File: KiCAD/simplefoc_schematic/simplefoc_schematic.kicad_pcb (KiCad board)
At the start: 2 copper layers, 52.3 x 49.1 mm, 61 parts, among them IC1 TMC6140-Trinamic, J1 Power Supply, J2 Motor Connector, J3 Sensor Connector, J5 Programming Port, J6 UART Port, J7 Servo, Q1 IRLR 2905, Q2 IRLR 2905, Q3 IRLR 2905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

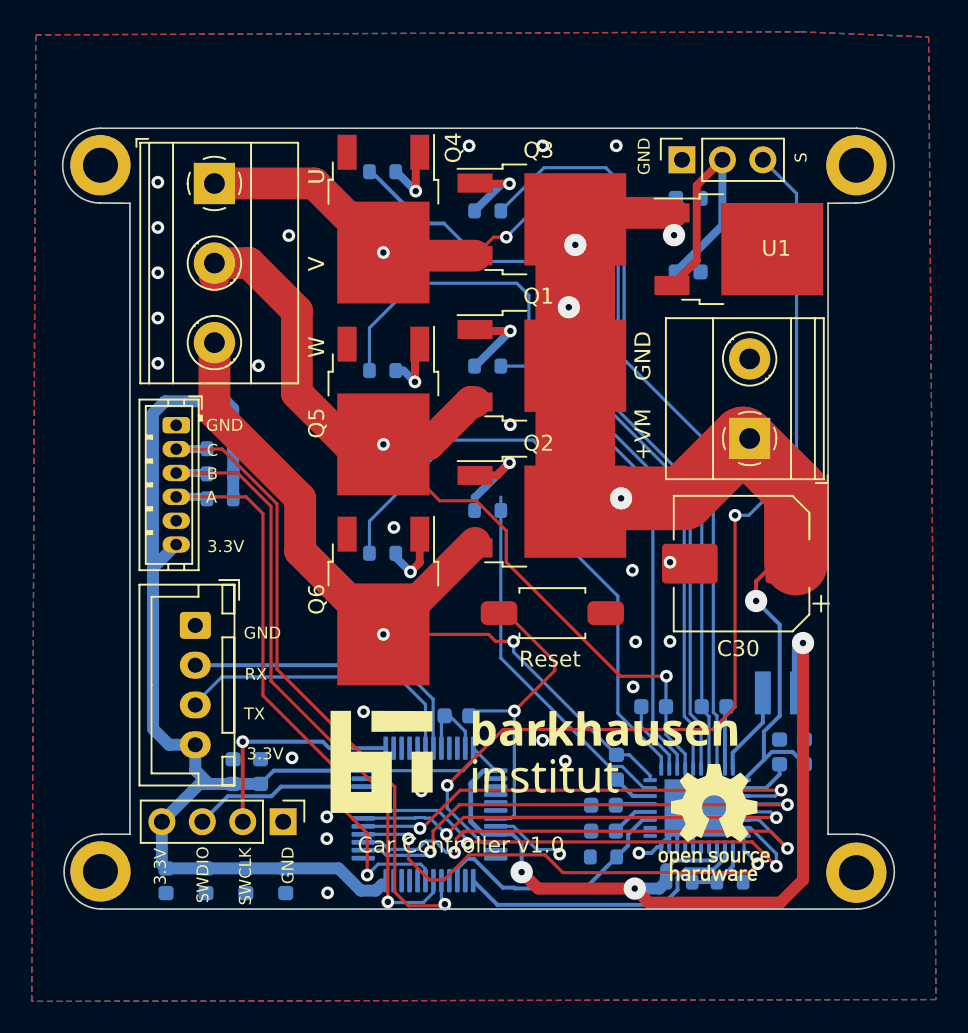
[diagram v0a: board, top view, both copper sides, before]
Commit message: Added second servo connection and fuse for servo
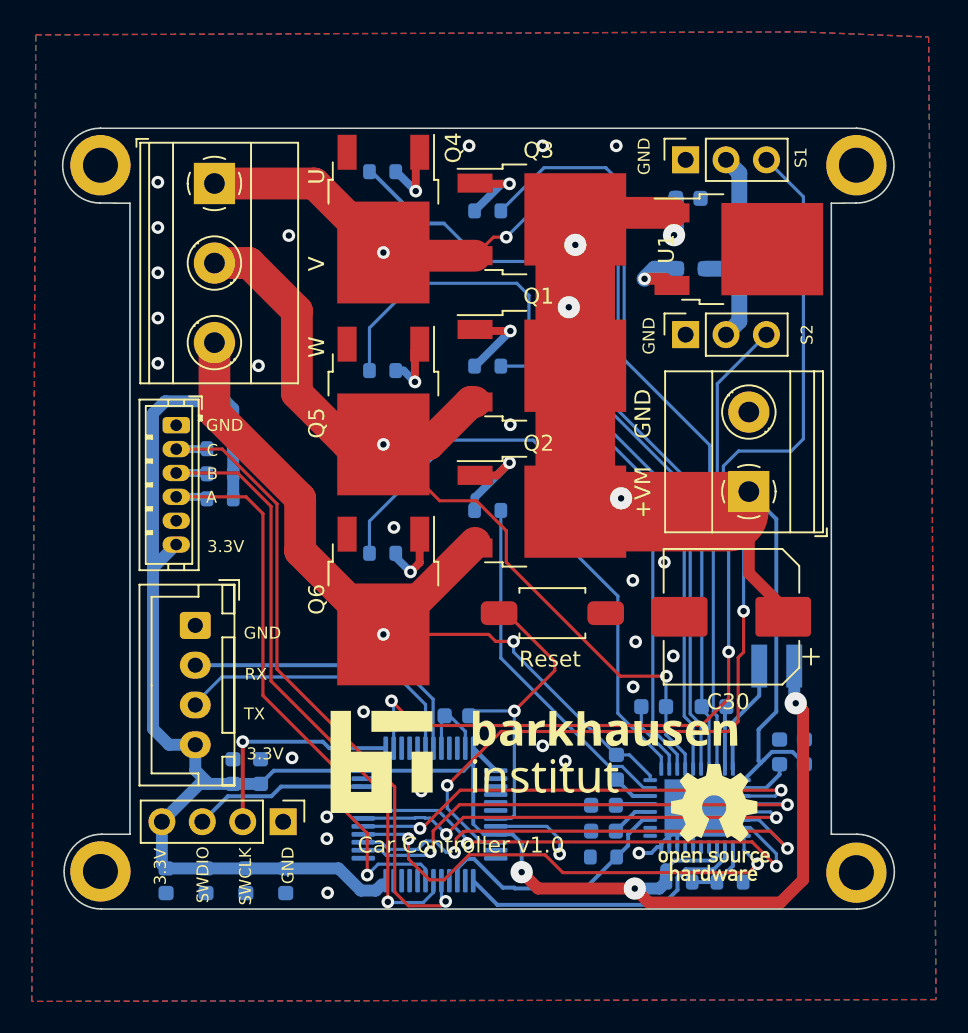
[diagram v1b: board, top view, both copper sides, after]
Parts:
- added F1: Polyfuse, Resistor_SMD:R_0603_1608Metric_Pad0.98x0.95mm_HandSolder, B.Cu at (113.3, 68.7)
- added J4: Servo, Connector_PinSocket_2.54mm:PinSocket_1x03_P2.54mm_Vertical, F.Cu at (112.9, 72.8)
- moved C19 3.99 mm to (117.1, 68.7)
- moved C30 3.40 mm to (115.8, 90.6)
- moved J1 3.34 mm to (116.9, 82.7)
- moved L1 1.70 mm to (118.6, 93.6)
- moved J7 0.23 mm to (112.9, 61.8)
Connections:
- net Servo renamed Servo1
- U1 pad 3: +5V -> Net-(U1-Pad3)
- U2 pad 38: unconnected-(U2-Pad38) -> Servo2
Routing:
- net Servo2: track 0.00 -> 50.0 mm, vias 0 -> 2
- net +BATT: track 80.2 -> 88.1 mm, vias 5 -> 4
- net +3.3V: track 134.8 -> 130.6 mm
- net Net-(U1-Pad3): track 0.00 -> 4.16 mm, vias 0 -> 1
- net +5V: track 17.5 -> 13.8 mm
- net Servo1: track 62.9 -> 66.3 mm
- net Net-(IC1-Pad10): track 5.57 -> 7.16 mm
- net V: track 60.1 -> 58.9 mm
- net GND: track 23.3 -> 24.2 mm
- net Net-(Q2-Pad1): track 5.59 -> 6.43 mm
- net HOUTW: track 22.9 -> 22.0 mm
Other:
- outline, holes or cut-outs redrawn
- board text added: "S1"
- board text added: "S2"
- board text removed: "S"

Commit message: Added polyfuse to battery input
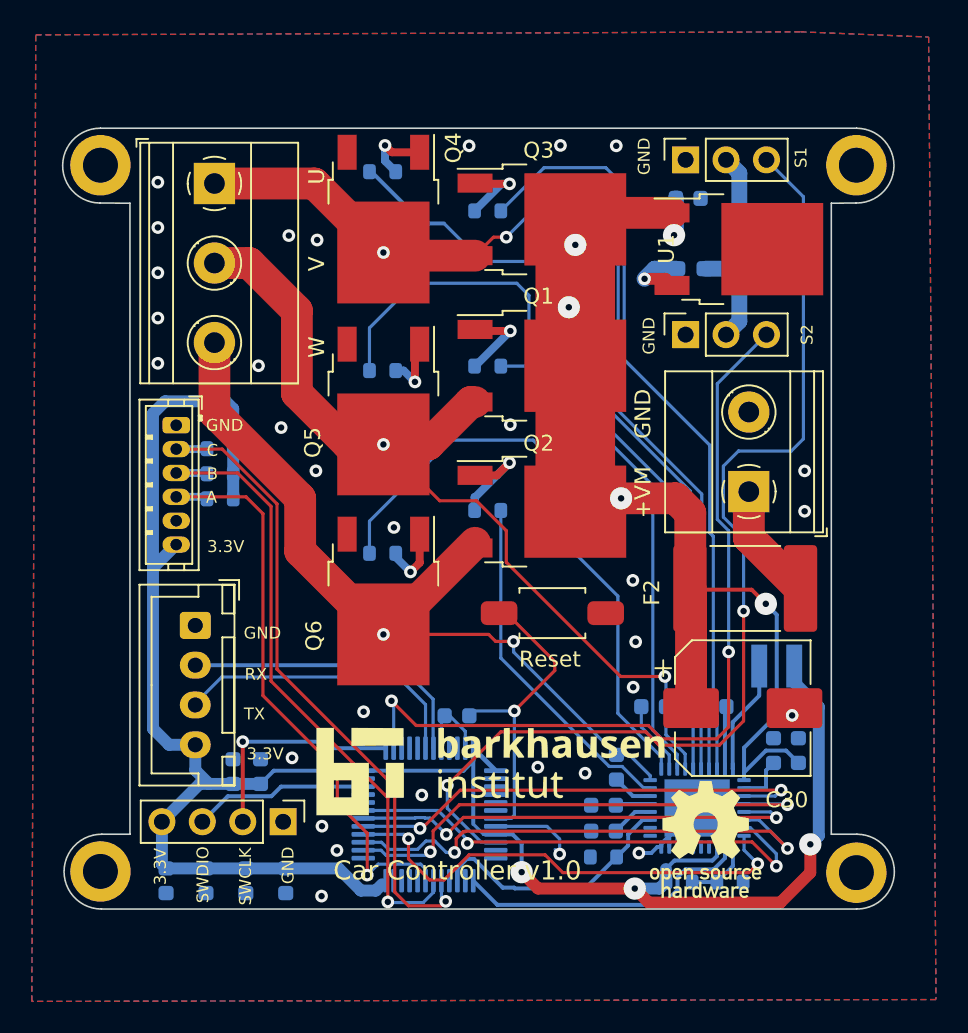
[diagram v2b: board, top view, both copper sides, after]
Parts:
- added F2: Polyfuse, Fuse:Fuse_2920_7451Metric_Pad2.10x5.45mm_HandSolder, F.Cu at (116.7, 88.8)
- F1: footprint Resistor_SMD:R_0603_1608Metric_Pad0.98x0.95mm_HandSolder -> Fuse:Fuse_0603_1608Metric_Pad1.05x0.95mm_HandSolder
- moved C30 5.78 mm to (116.5, 96.3), turned to 0 degrees
- moved G*** 2.79 mm to (100.6, 100.3)
- moved G*** 1.19 mm to (114.2, 104.5)
- moved C23 0.39 mm to (120.0, 99.0)
- moved C27 0.39 mm to (118.4, 99.0)
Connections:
- J1 pad 1: +BATT -> Net-(J1-Pad1)
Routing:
- net Net-(J1-Pad1): track 0.00 -> 7.52 mm
- net +BATT: track 88.1 -> 83.2 mm, vias 4 -> 5
- net Servo2: track 50.0 -> 51.7 mm
- net Servo1: track 66.3 -> 67.1 mm
- net +3.3V: track 130.6 -> 131.4 mm
- net GND: vias 27 -> 31

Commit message: Change to 4 Layer PCB with better grounding
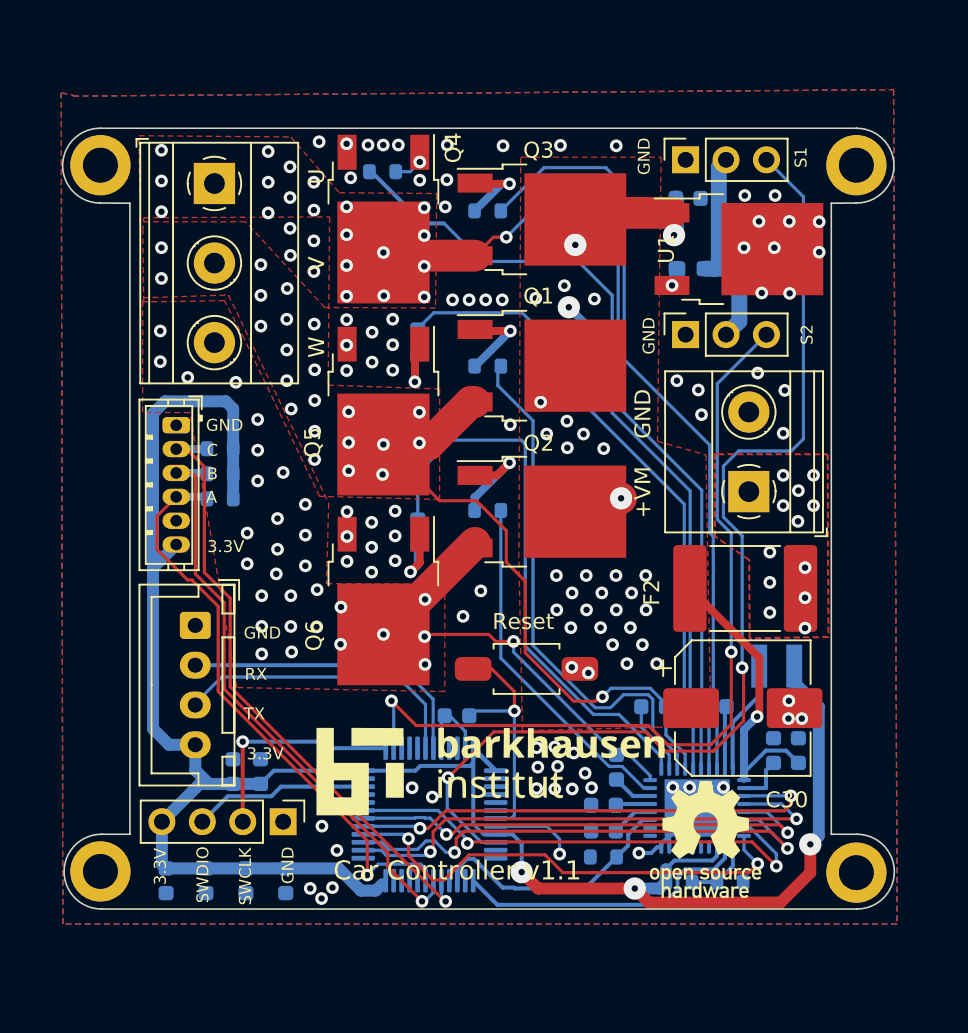
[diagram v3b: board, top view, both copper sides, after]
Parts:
- moved SW1 3.86 mm to (102.9, 93.8)
- moved R6 2.85 mm to (96.1, 73.3), turned to -90 degrees
- moved R11 2.59 mm to (96.1, 85.2), turned to -90 degrees
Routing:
- net +BATT: track 83.2 -> 45.5 mm, vias 5 -> 32
- net W: track 54.2 -> 31.4 mm, vias 2 -> 31
- net V: track 58.8 -> 42.8 mm, vias 2 -> 23
- net U: track 70.5 -> 58.0 mm, vias 2 -> 25
- net LOUTV: track 48.2 -> 40.1 mm
- net Net-(J1-Pad1): track 7.52 -> 0.00 mm, vias 0 -> 12
- net Net-(C4-Pad1): track 19.9 -> 15.2 mm
- net ENCC: track 42.2 -> 39.2 mm
- net ENCB: track 40.6 -> 37.5 mm
- net Net-(U1-Pad3): track 4.16 -> 1.18 mm
- net LOUTW: track 38.4 -> 35.5 mm
- net Net-(Q4-Pad1): track 4.29 -> 1.76 mm
- net HOUTV: track 31.1 -> 33.2 mm
- net HO2: track 29.0 -> 30.9 mm
- net ENCA: track 38.1 -> 36.7 mm
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- added copper zone on F.Cu, net +BATT
- added copper zone on In2.Cu, net +BATT
- added copper zone on In1.Cu, net GND
- added copper zone on In2.Cu, net GND
- added copper zone on F.Cu, net Net-(J1-Pad1)
- added copper zone on In1.Cu, net Net-(J1-Pad1)
- added copper zone on In2.Cu, net Net-(J1-Pad1)
- added copper zone on F.Cu, net U
- added copper zone on In2.Cu, net U
- added copper zone on F.Cu, net V
- added copper zone on In2.Cu, net V
- added copper zone on F.Cu, net W
- added copper zone on In2.Cu, net W
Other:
- copper layers 2 -> 4
- board text added: "Car Controller v1.1"
- board text removed: "Car Controller v1.0"
